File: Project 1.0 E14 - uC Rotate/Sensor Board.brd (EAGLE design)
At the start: 38.5 x 75 mm, 107 parts, among them IC1 LT1963EST-1.5, IC2 LT1963EST-1.5, IC4 LT1963EST-1.5, J1 501568-0207, J2 501568-0207, J3 SD-105027-101, U1 MAG3110, U10 ADXL362, U11 TM4C1233H6PM, U14 TXB0108, U15 ADT7301, U17 LSM9DS0, U19 MAX21000, U2 H3LIS331DLTR, U21 SN74HC42, U22 SI7013, U3 L3GD20H, U4 LPS331AP, U5 MPL3115A2, U6 LSM303D, U7 501568-0407, U8 STLM20, U9 LIS3DH

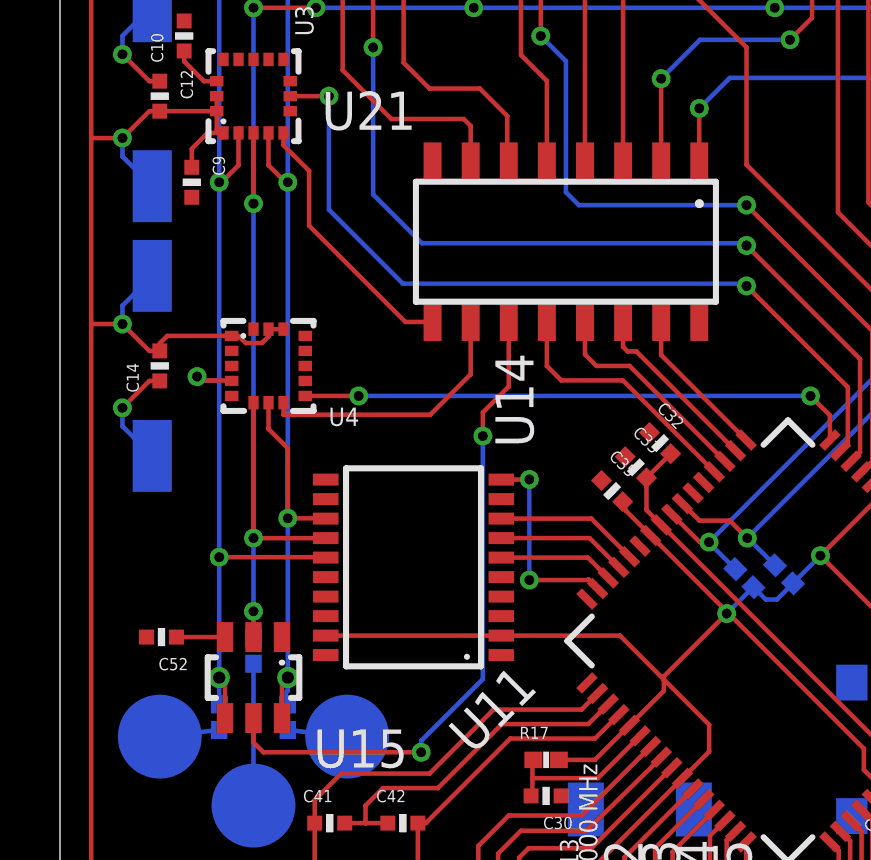
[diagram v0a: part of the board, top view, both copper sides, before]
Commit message: Sensor Test Board: Moved connections on TXB0108 to allow for simpler grounding of unused connections
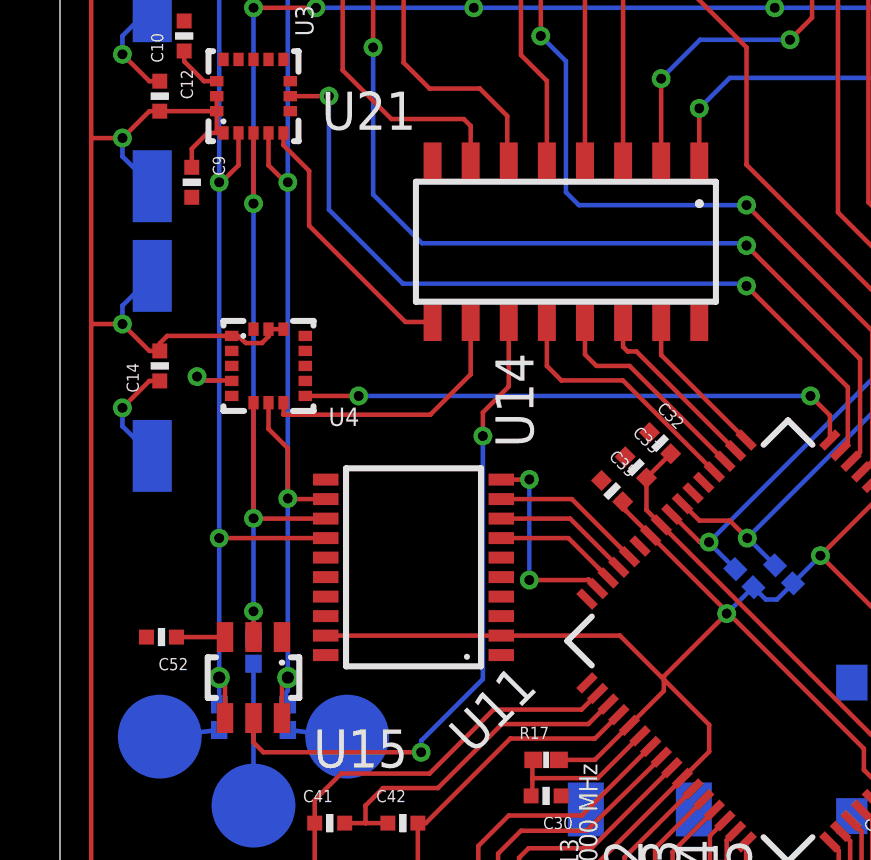
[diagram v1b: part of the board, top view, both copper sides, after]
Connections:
- net GND: now also U14.P$1, U14.P$15, U14.P$16, U14.P$17, U14.P$18, U14.P$20, U14.P$3, U14.P$4, U14.P$5, U14.P$6
- net MISO-A: now also U14.P$9; no longer U14.P$8
- net MISO-B: now also U14.P$12; no longer U14.P$13
- net MOSI-A: now also U14.P$8; no longer U14.P$7
- net MOSI-B: now also U14.P$13; no longer U14.P$14
- net SCLK-A: now also U14.P$7; no longer U14.P$6
- net SCLK-B: now also U14.P$14; no longer U14.P$15
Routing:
- net MOSI-B: track 97.4 -> 96.7 mm
- net MISO-B: track 92.0 -> 91.3 mm

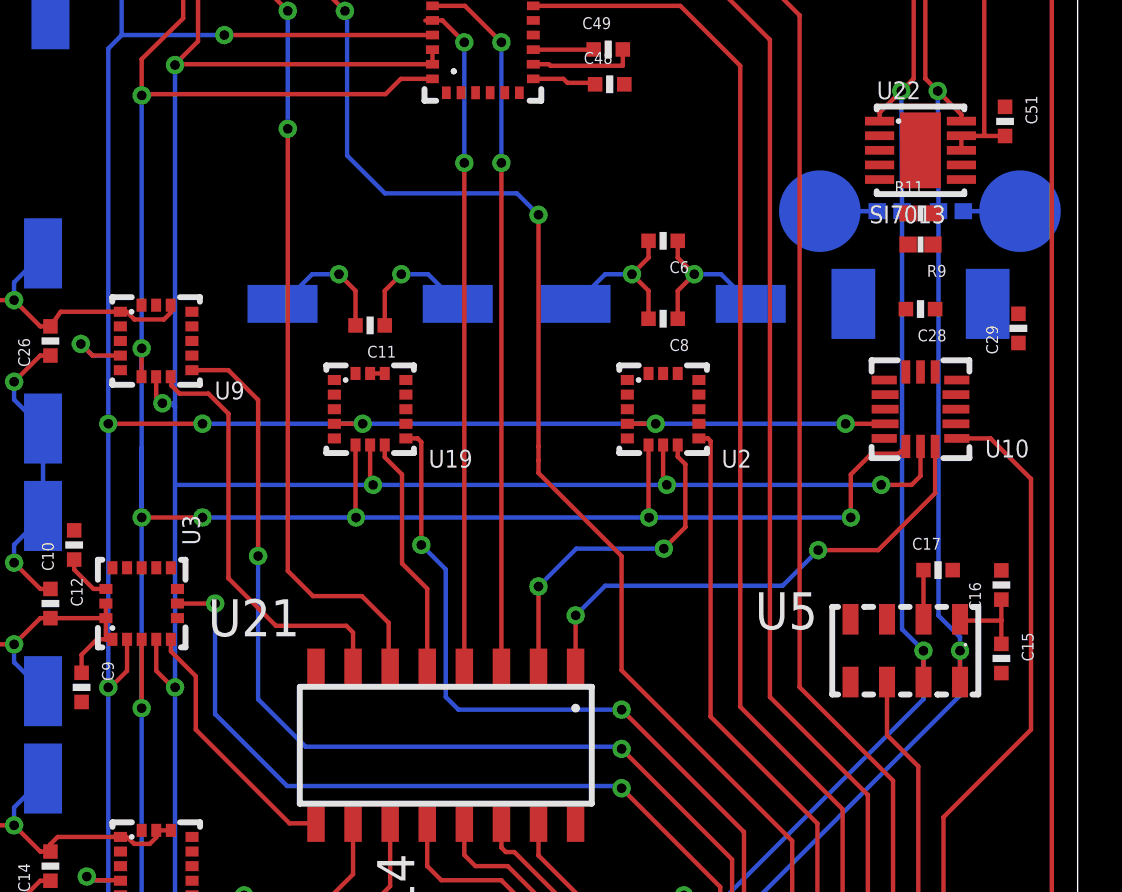
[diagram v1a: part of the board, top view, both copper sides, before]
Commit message: Sensor Test Board: Resolved issue 22 by changing from LSG3 INT1 to INT2 allowing for an interupt to be genarated on a watermark event
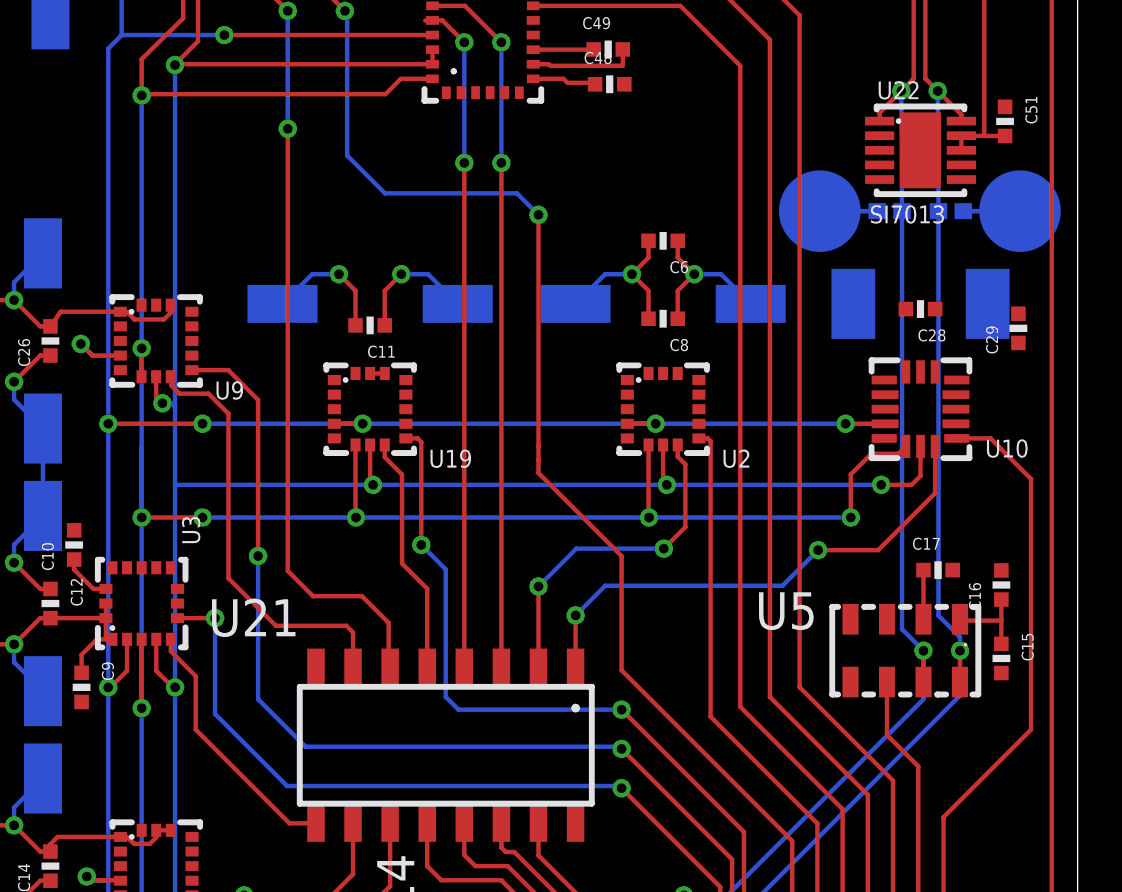
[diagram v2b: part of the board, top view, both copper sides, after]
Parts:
- removed R11: 1.0k, Kas-Passives:R0402
- removed R9: 2.0k, Kas-Passives:R0402
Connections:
- removed net INT1-L3GD: U11.P$15, U3.P$7
- removed net N$2: R11.2, R9.1, U22.P$6
- new net INT2-L3GD: U11.P$15, U3.P$6
- net GND: no longer R11.1, U22.P$7
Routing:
- net INT1-L3GD: track 27.0 -> 0.00 mm, vias 2 -> 0
- net INT2-L3GD: track 0.00 -> 26.5 mm, vias 0 -> 2
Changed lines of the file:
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@@
 <element name="R8" library="Kas-Passives" package="R0402" value="0" x="33.5622" y="59.055" rot="MR0"/>
 <element name="U22" library="Kas-Sensors" package="DFN-10(3X3)" value="SI7013" x="34.6202" y="61.1378"/>
-<element name="R9" library="Kas-Passives" package="R0402" value="2.0k" x="34.6202" y="57.912" rot="R180"/>
-<element name="R11" library="Kas-Passives" package="R0402" value="1.0k" x="34.6202" y="58.9788"/>
 <element name="C51" library="Kas-Passives" package="C0402" value="" x="37.5158" y="62.1284" rot="R270"/>
 <element name="J1" library="Kas-Connectors" package="501568-0207" value="501568-0207" x="6.9088" y="17.7292" rot="MR180"/>
@@
 <contactref element="U11" pad="P$32"/>
 <contactref element="U3" pad="P$8"/>
-<contactref element="U22" pad="P$7"/>
-<contactref element="R11" pad="1"/>
 <contactref element="U17" pad="P$11"/>
 <wire x1="16.2306" y1="24.6888" x2="14.097" y2="22.5552" width="0.1524" layer="1"/>
@@
 <wire x1="37.5332" y1="67.564" x2="35.9868" y2="69.1532" width="0" layer="19" extent="1-1"/>
 <wire x1="37.5158" y1="62.6284" x2="37.5332" y2="67.564" width="0" layer="19" extent="1-1"/>
-<wire x1="36.0202" y1="60.6378" x2="37.5158" y2="62.6284" width="0" layer="19" extent="1-1"/>
-<wire x1="34.1952" y1="58.9788" x2="36.0202" y2="60.6378" width="0" layer="19" extent="1-1"/>
-<wire x1="33.2202" y1="60.6378" x2="34.1952" y2="58.9788" width="0" layer="19" extent="1-1"/>
-<wire x1="33.2202" y1="61.1378" x2="33.2202" y2="60.6378" width="0" layer="19" extent="1-1"/>
-<wire x1="33.2202" y1="61.6378" x2="33.2202" y2="61.1378" width="0" layer="19" extent="1-1"/>
-<wire x1="34.1202" y1="55.7022" x2="34.1952" y2="58.9788" width="0" layer="19" extent="1-1"/>
-<wire x1="32.3202" y1="55.88" x2="34.1202" y2="55.7022" width="0" layer="19" extent="1-16"/>
+<wire x1="33.2202" y1="61.6378" x2="37.5158" y2="62.6284" width="0" layer="19" extent="1-1"/>
+<wire x1="33.2202" y1="61.1378" x2="33.2202" y2="61.6378" width="0" layer="19" extent="1-1"/>
+<wire x1="33.2202" y1="60.6378" x2="33.2202" y2="61.1378" width="0" layer="19" extent="1-1"/>
+<wire x1="32.3202" y1="55.88" x2="33.2202" y2="60.6378" width="0" layer="19" extent="1-16"/>
+<wire x1="34.1202" y1="55.7022" x2="32.3202" y2="55.88" width="0" layer="19" extent="1-16"/>
 <wire x1="34.1202" y1="53.5482" x2="34.1202" y2="55.7022" width="0" layer="19" extent="1-1"/>
 <wire x1="35.8627" y1="53.2732" x2="34.1202" y2="53.5482" width="0" layer="19" extent="1-1"/>
@@
 <wire x1="6.2998" y1="46.1184" x2="6.7252" y2="46.1184" width="0.1524" layer="1"/>
 </signal>
-<signal name="INT1-L3GD">
-<contactref element="U3" pad="P$7"/>
+<signal name="INT2-L3GD">
 <contactref element="U11" pad="P$15"/>
-<via x="10.4648" y="45.6184" extent="1-16" drill="0.3302"/>
-<wire x1="10.4648" y1="45.6184" x2="9.1752" y2="45.6184" width="0.1524" layer="1"/>
+<via x="10.4648" y="45.1184" extent="1-16" drill="0.3302"/>
 <via x="24.384" y="39.2938" extent="1-16" drill="0.3302" diameter="0.254"/>
 <wire x1="24.384" y1="39.2938" x2="24.3332" y2="39.37" width="0.1524" layer="16"/>
 <wire x1="24.3332" y1="39.37" x2="12.9286" y2="39.37" width="0.1524" layer="16"/>
 <wire x1="12.9286" y1="39.37" x2="10.4648" y2="41.8338" width="0.1524" layer="16"/>
-<wire x1="10.4648" y1="41.8338" x2="10.4648" y2="45.6184" width="0.1524" layer="16"/>
+<wire x1="10.4648" y1="41.8338" x2="10.4648" y2="45.1184" width="0.1524" layer="16"/>
 <wire x1="27.5170875" y1="33.80448125" x2="27.7622" y2="34.04959375" width="0.1524" layer="1"/>
 <wire x1="27.7622" y1="34.04959375" x2="27.7622" y2="35.9156" width="0.1524" layer="1"/>
 <wire x1="27.7622" y1="35.9156" x2="24.384" y2="39.2938" width="0.1524" layer="1"/>
+<contactref element="U3" pad="P$6"/>
+<wire x1="10.4648" y1="45.1184" x2="9.1752" y2="45.1184" width="0.1524" layer="1"/>
 </signal>
 <signal name="N$5">
@@
 <signal name="VSNS">
 </signal>
-<signal name="N$2">
-<contactref element="R9" pad="1"/>
-<contactref element="R11" pad="2"/>
-<contactref element="U22" pad="P$6"/>
-<wire x1="35.0452" y1="58.9788" x2="36.0202" y2="60.1378" width="0" layer="19" extent="1-1"/>
-<wire x1="35.0452" y1="57.912" x2="35.0452" y2="58.9788" width="0" layer="19" extent="1-1"/>
-</signal>
 <signal name="U6TX">

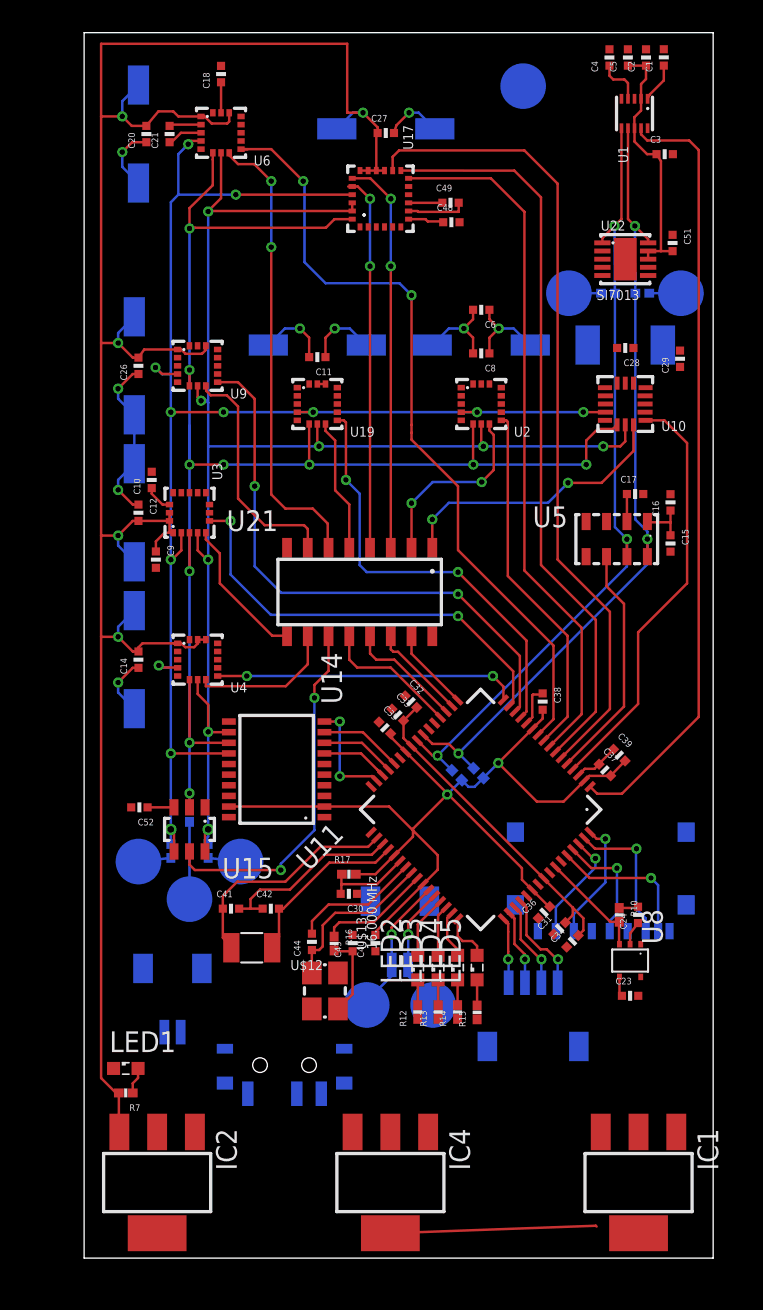
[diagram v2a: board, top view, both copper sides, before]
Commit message: Sensor Test Board: Added power lines for all components. Split power into two groups A (130 mA) and B (177 mA). A has sensors connected except for the STLM20. B has the remaing components.  I2C test points were moved to allow for power routing to the right side sensors. Intterupt lines for ADXL362 and MPL3115A2 where swapped to allow for easier power routing
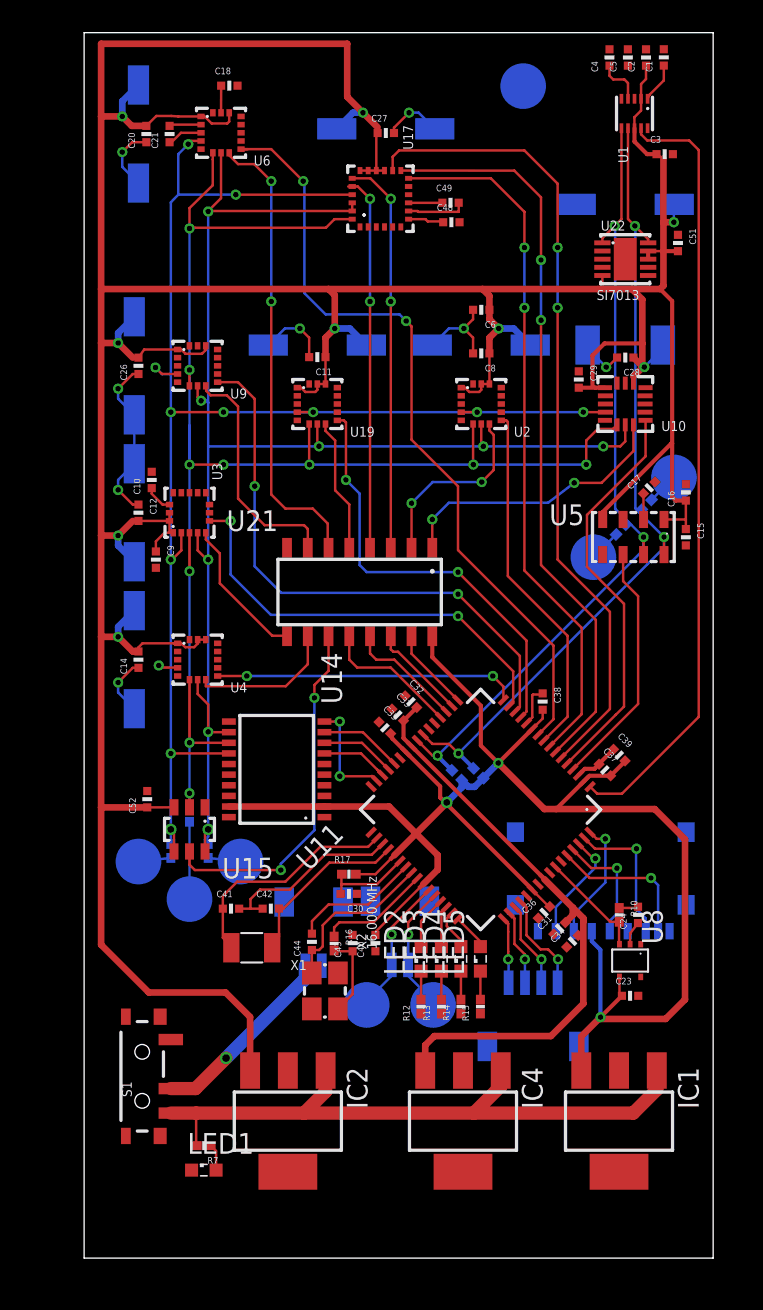
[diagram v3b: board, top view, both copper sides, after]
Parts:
- added C22: 10uF, Kas-Passives:4.3X7.3SMD
- moved TP5 16.2 mm to (32.7, 42.9), turned to 225 degrees
- moved R8 14.5 mm to (34.4, 44.6), turned to 315 degrees
- moved R5 13.0 mm to (35.9, 46.1), turned to 135 degrees
- moved TP6 11.3 mm to (37.6, 47.8), turned to 225 degrees
- moved J1 9.54 mm to (15.5, 21.8)
- moved IC2 8.84 mm to (14.0, 8.38)
- moved S1 8.74 mm to (5.05, 11.1), flipped to the top, turned to 90 degrees
- moved LED1 7.84 mm to (8.83, 5.38)
- moved C29 6.33 mm to (31.8, 53.8), turned to 270 degrees
- moved IC4 5.82 mm to (24.7, 8.38)
- moved R7 5.76 mm to (8.83, 6.88)
- moved IC1 3.94 mm to (34.2, 8.38)
- moved C16 1.12 mm to (38.3, 46.9)
- moved U5 1.02 mm to (35.1, 44.1)
- moved C15 1.01 mm to (38.3, 44.1)
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- renumbered U$12 to X1, U$13 to X2, U7 to J4
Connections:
- removed net 3.3V: C11.1, C12.2, C13.P$1, C14.2, C15.1, C16.1, C19.P$1, C2.1, C20.2, C23.1, C25.P$1, C26.2, C27.1, C28.1, C29.2, C3.1, C35.2, C36.2, C37.2, C38.2, C39.2, C40.2, C45.P$1, C46.P$1, C47.P$1, C5.1, C51.2, C52.1, C54.P$1, C6.1, C7.P$1, C8.1, C9.1, IC2.3, J3.P$4, R1.2, R17.2, R2.2, R7.2, U1.P$2, U1.P$8, U10.P$1, U10.P$14, U11.P$11, U11.P$2, U11.P$26, U11.P$37, U11.P$42, U11.P$54, U14.P$19, U14.P$2, U15.P$3, U17.P$15, U17.P$16, U17.P$17, U17.P$18, U19.P$1, U19.P$14, U19.P$15, U2.P$1, U2.P$14, U2.P$15, U21.P$16, U22.P$5, U22.P$8, U22.P$9, U3.P$1, U3.P$15, U3.P$16, U4.P$1, U4.P$14, U4.P$15, U5.P$1, U5.P$4, U6.P$1, U6.P$14, U8.P$4, U9.P$1, U9.P$14
- removed net LSM9D-DEN-G: U17.P$10
- removed net N$23: IC1.1, IC2.1, IC4.1, S1.1
- new net 3.3V-A: C11.1, C12.2, C13.P$1, C14.2, C15.1, C16.1, C19.P$1, C2.1, C20.2, C22.P$2, C25.P$1, C26.2, C27.1, C28.1, C29.2, C3.1, C45.P$1, C46.P$1, C47.P$1, C5.1, C51.2, C52.1, C54.P$1, C6.1, C7.P$1, C8.1, C9.1, IC2.3, U1.P$2, U1.P$8, U10.P$1, U10.P$14, U15.P$3, U17.P$15, U17.P$16, U17.P$17, U17.P$18, U19.P$1, U19.P$14, U19.P$15, U2.P$1, U2.P$14, U2.P$15, U22.P$5, U22.P$8, U22.P$9, U3.P$1, U3.P$15, U3.P$16, U4.P$1, U4.P$14, U4.P$15, U5.P$1, U5.P$4, U6.P$1, U6.P$14, U9.P$1, U9.P$14
- new net 3.3V-B: C23.1, C35.2, C36.2, C37.2, C38.2, C39.2, C40.2, IC1.3, J3.P$4, R1.2, R17.2, R2.2, U11.P$11, U11.P$2, U11.P$26, U11.P$37, U11.P$42, U11.P$54, U14.P$19, U14.P$2, U21.P$16, U8.P$4
- new net POWER-IN: IC1.1, IC2.1, IC4.1, R7.2, S1.1
- net GND: now also C22.P$1, J1.P$2, U17.P$10; no longer J1.P$1, U17.P$11
- net INT1-MPL311: now also U11.P$4; no longer U11.P$5
- net INT2-ADXL362: now also U11.P$5; no longer U11.P$4
- net N$19: now also J1.P$1; no longer J1.P$2
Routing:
- net 3.3V-A: track 0.00 -> 257.4 mm, vias 0 -> 9
- net 3.3V: track 229.2 -> 0.00 mm, vias 9 -> 0
- net 3.3V-B: track 0.00 -> 110.9 mm, vias 0 -> 3
- net POWER-IN: track 0.00 -> 40.0 mm
- net 1.2V: track 20.2 -> 37.5 mm
- net N$19: track 0.00 -> 11.8 mm, vias 0 -> 1
- net GND: track 70.5 -> 60.6 mm, vias 7 -> 8
- net SDA-0: track 49.0 -> 50.2 mm
- net SCL-0: track 49.9 -> 51.1 mm
- net INT2-ADXL362: track 26.0 -> 24.9 mm
- net IND-LED-4: track 3.06 -> 2.36 mm
- net INT1-MPL311: track 14.6 -> 15.2 mm
- net IND-LED-1: track 3.86 -> 3.25 mm
- net IND-LED-2: track 3.14 -> 2.52 mm
- net LSM9D-INT2-XM: vias 0 -> 2
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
